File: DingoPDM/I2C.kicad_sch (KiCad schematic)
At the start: 10 parts, among them U5 MB85RC256V, U6 MCP9808

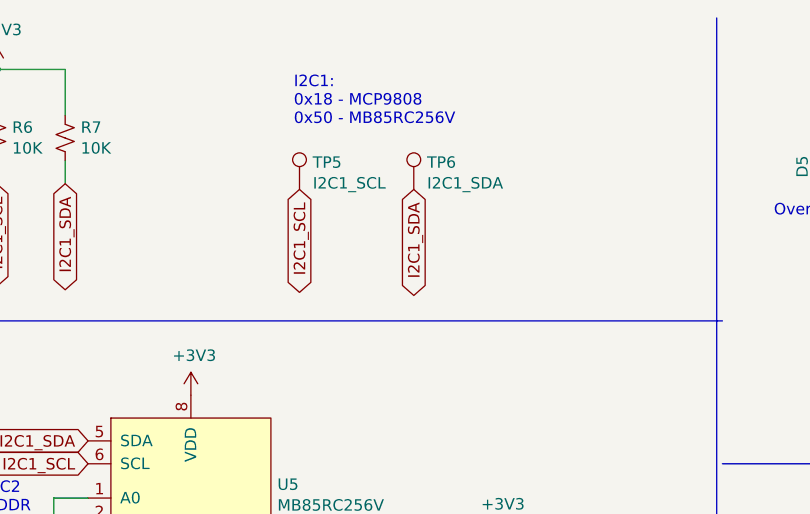
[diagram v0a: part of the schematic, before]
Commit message: Modified PCB for 10ch PDM board
I modified the original dingoPDM for 10 channels. The board has been manufactured, tested and works but after mounting I decided that it doesn't suit my needs for the current build. I may develop it further in the future, make it pretty etc but for now I am marking this project as stale.
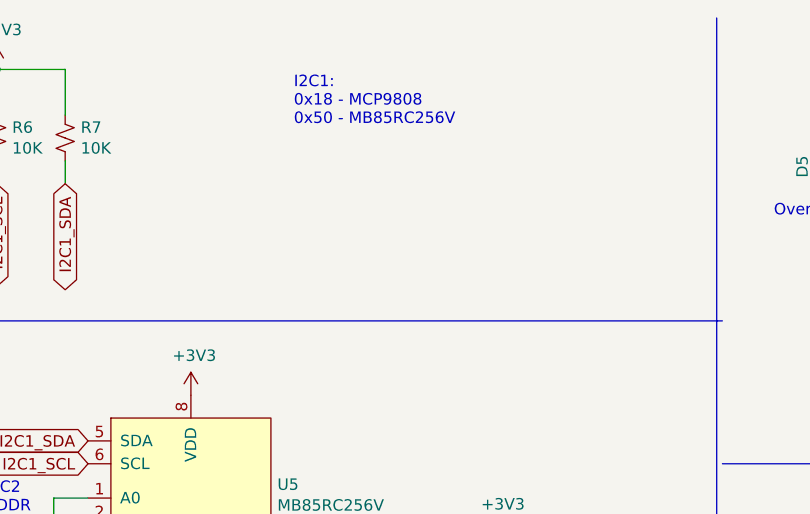
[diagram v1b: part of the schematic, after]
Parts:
- removed TP5: I2C1_SCL, TestPoint:TestPoint_Keystone_5000-5004_Miniature, symbol Connector:TestPoint
- removed TP6: I2C1_SDA, TestPoint:TestPoint_Keystone_5000-5004_Miniature, symbol Connector:TestPoint
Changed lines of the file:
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@@
-		)
-	)
-	(global_label "I2C1_SDA"
-		(shape bidirectional)
-		(at 63.5 31.75 270)
-		(fields_autoplaced yes)
-		(effects
-			(font
-				(size 1.27 1.27)
-			)
-			(justify right)
-		)
-		(property "Intersheetrefs" "${INTERSHEET_REFS}"
-			(at 63.5 43.7836 90)
-			(effects
-				(font
-					(size 1.27 1.27)
-				)
-				(justify right)
-				(hide yes)
-			)
-		)
-	)
-	(global_label "I2C1_SCL"
-		(shape bidirectional)
-		(at 50.8 31.75 270)
-		(fields_autoplaced yes)
-		(effects
-			(font
-				(size 1.27 1.27)
-			)
-			(justify right)
-		)
-		(property "Intersheetrefs" "${INTERSHEET_REFS}"
-			(at 50.8 43.7231 90)
-			(effects
-				(font
-					(size 1.27 1.27)
-				)
-				(justify right)
-				(hide yes)
-			)
 		)
 	)
@@
 					(unit 1)
 				)
-			)
-		)
-	)
-	(symbol
-		(lib_id "Connector:TestPoint")
-		(at 50.8 31.75 0)
-		(unit 1)
-		(exclude_from_sim no)
-		(in_bom yes)
-		(on_board yes)
-		(dnp no)
-		(property "Reference" "TP5"
-			(at 52.2732 28.7528 0)
-			(effects
-				(font
-					(size 1.27 1.27)
-				)
-				(justify left)
-			)
-		)
-		(property "Value" "I2C1_SCL"
-			(at 52.2732 31.0642 0)
-			(effects
-				(font
-					(size 1.27 1.27)
-				)
-				(justify left)
-			)
-		)
-		(property "Footprint" "TestPoint:TestPoint_Keystone_5000-5004_Miniature"
-			(at 55.88 31.75 0)
-			(effects
-				(font
-					(size 1.27 1.27)
-				)
-				(hide yes)
-			)
-		)
-		(property "Datasheet" ""
-			(at 55.88 31.75 0)
-			(effects
-				(font
-					(size 1.27 1.27)
-				)
-				(hide yes)
-			)
-		)
-		(property "Description" ""
-			(at 50.8 31.75 0)
-			(effects
-				(font
-					(size 1.27 1.27)
-				)
-				(hide yes)
-			)
-		)
-		(property "LCSC" ""
-			(at 50.8 31.75 0)
-			(effects
-				(font
-					(size 1.27 1.27)
-				)
-				(hide yes)
-			)
-		)
-		(pin "1"
-		)
-		(instances
-			(project "DingoPDM"
-				(path "/8948e307-9174-4227-9c28-3ff885e6e83d/00000000-0000-0000-0000-00005f5b7065"
-					(reference "TP5")
-					(unit 1)
-				)
-			)
-		)
-	)
-	(symbol
-		(lib_id "Connector:TestPoint")
-		(at 63.5 31.75 0)
-		(unit 1)
-		(exclude_from_sim no)
-		(in_bom yes)
-		(on_board yes)
-		(dnp no)
-		(property "Reference" "TP6"
-			(at 64.9732 28.7528 0)
-			(effects
-				(font
-					(size 1.27 1.27)
-				)
-				(justify left)
-			)
-		)
-		(property "Value" "I2C1_SDA"
-			(at 64.9732 31.0642 0)
-			(effects
-				(font
-					(size 1.27 1.27)
-				)
-				(justify left)
-			)
-		)
-		(property "Footprint" "TestPoint:TestPoint_Keystone_5000-5004_Miniature"
-			(at 68.58 31.75 0)
-			(effects
-				(font
-					(size 1.27 1.27)
-				)
-				(hide yes)
-			)
-		)
-		(property "Datasheet" ""
-			(at 68.58 31.75 0)
-			(effects
-				(font
-					(size 1.27 1.27)
-				)
-				(hide yes)
-			)
-		)
-		(property "Description" ""
-			(at 63.5 31.75 0)
-			(effects
-				(font
-					(size 1.27 1.27)
-				)
-				(hide yes)
-			)
-		)
-		(property "LCSC" ""
-			(at 63.5 31.75 0)
-			(effects
-				(font
-					(size 1.27 1.27)
-				)
-				(hide yes)
-			)
-		)
-		(pin "1"
-		)
-		(instances
-			(project "DingoPDM"
-				(path "/8948e307-9174-4227-9c28-3ff885e6e83d/00000000-0000-0000-0000-00005f5b7065"
-					(reference "TP6")
-					(unit 1)
-				)
